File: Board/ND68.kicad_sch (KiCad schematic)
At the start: 4 parts

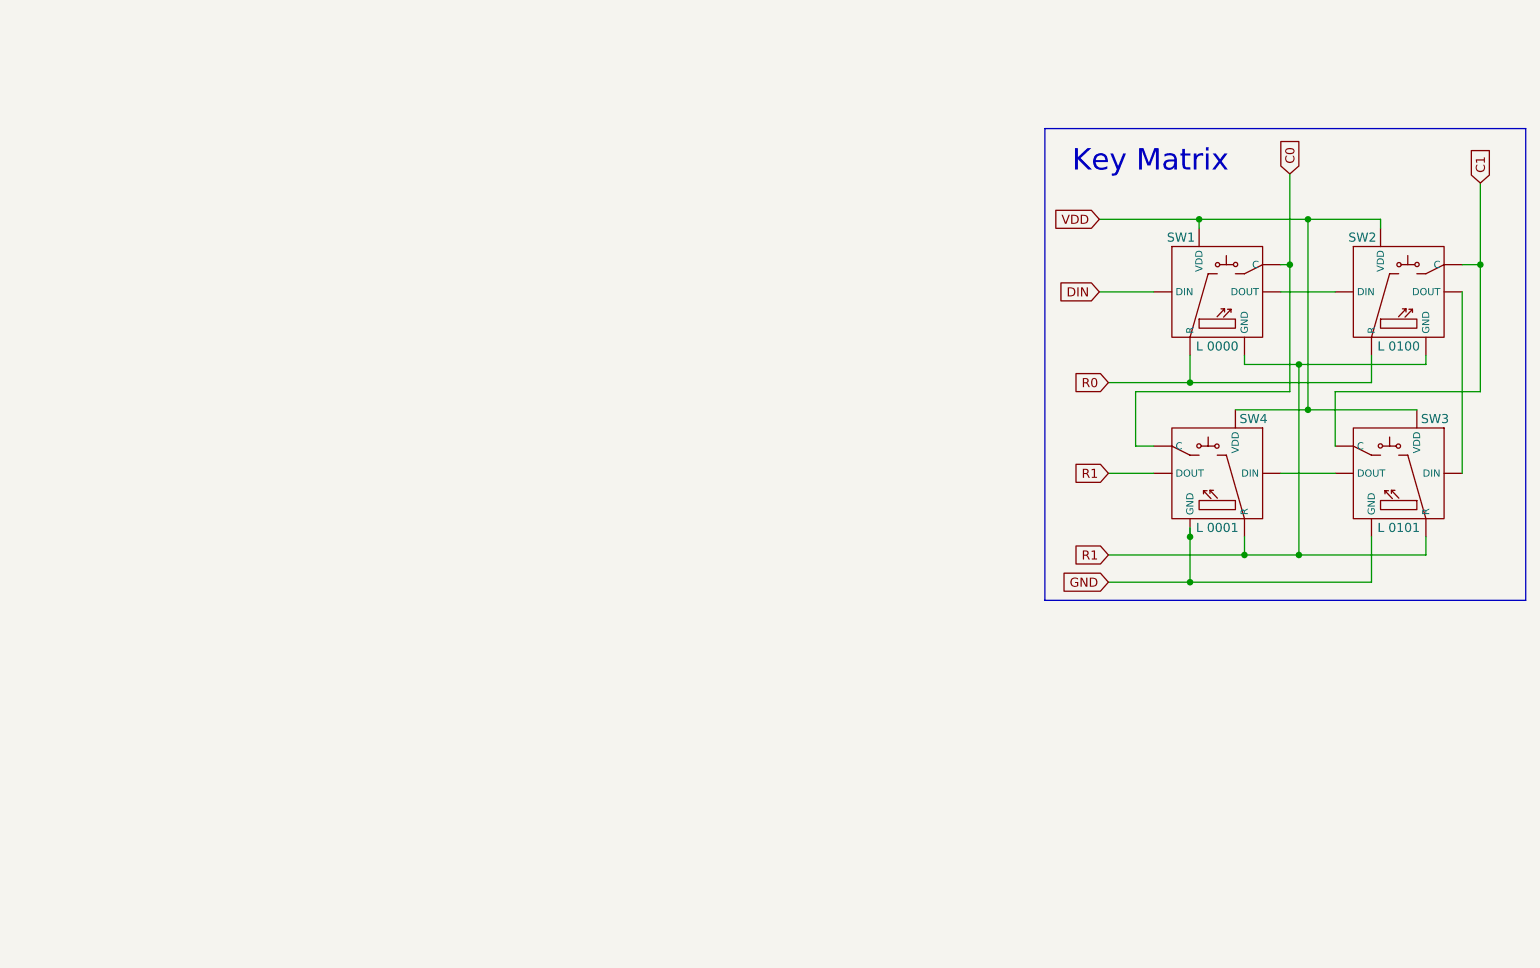
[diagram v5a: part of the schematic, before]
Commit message: Cleaned up key matrix and added diodes
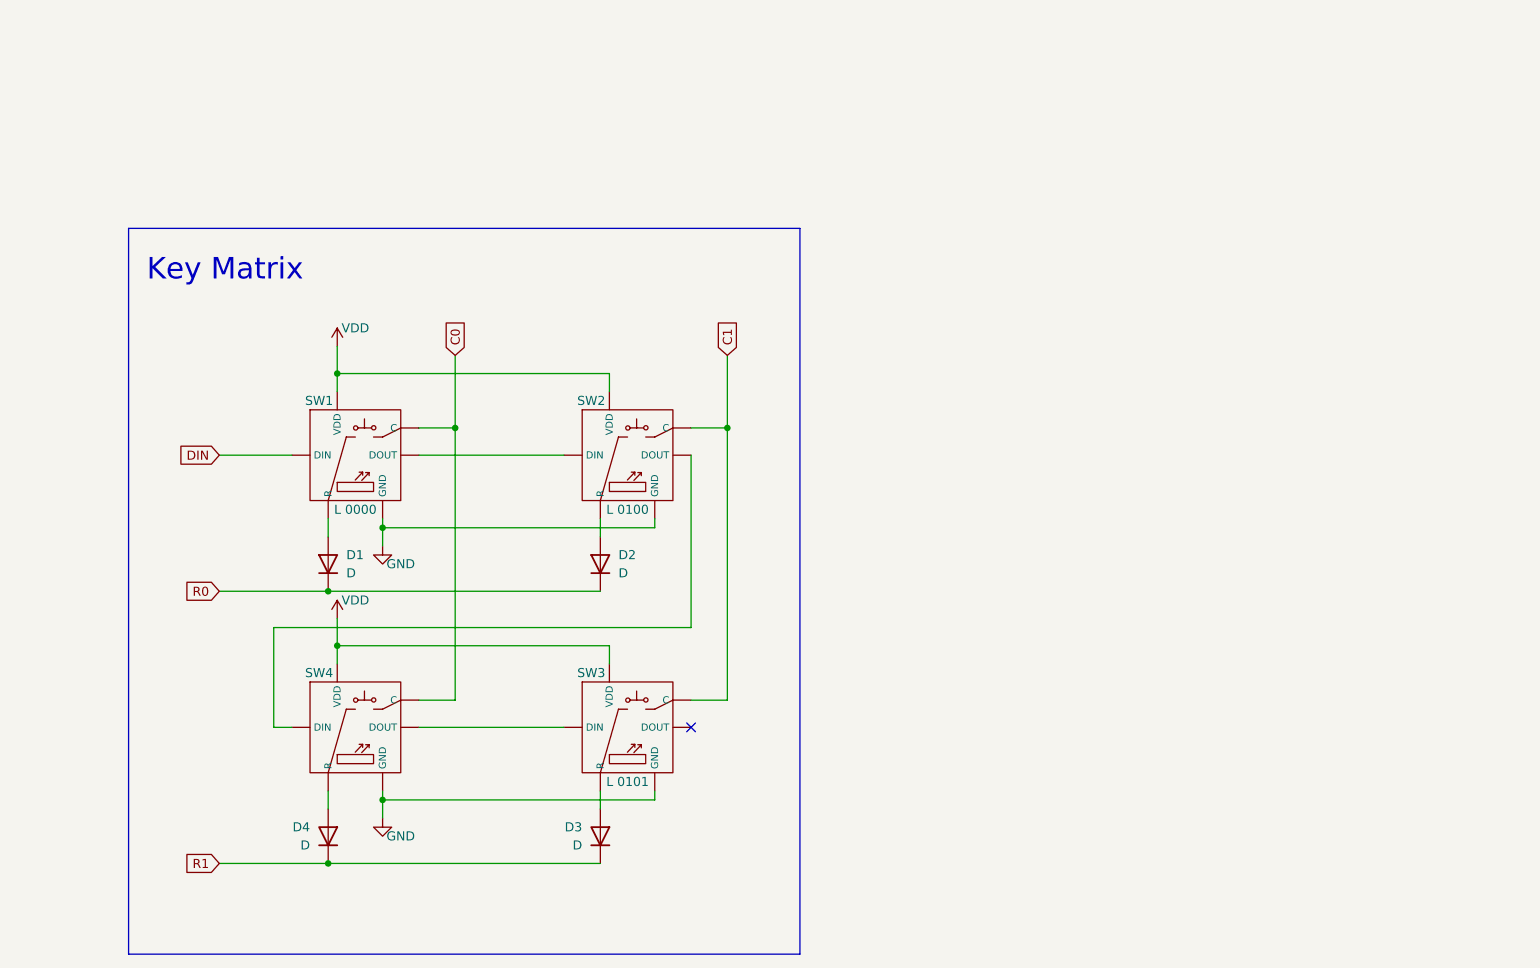
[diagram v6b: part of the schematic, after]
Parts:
- added D1, D2, D3, D4: D, Diode_SMD:D_SOD-123F, symbol Device:D
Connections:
- net GND: now also SW1. (VDD), SW2. (VDD)
- net R0: now also D1.1 (K), D2.1 (K); no longer SW1. (VDD), SW2. (VDD)
- net R1: now also D3.1 (K), D4.1 (K); no longer SW1. (VDD), SW2. (VDD), SW3. (VDD), SW4. (VDD)
- new net: SW3. (VDD), SW4. (VDD)
- new net: SW2. (VDD), SW4. (VDD)
- new net: D4.2 (A), SW4. (VDD)
- new net: D3.2 (A), SW3. (VDD)
- new net: D2.2 (A), SW2. (VDD)
- new net: D1.2 (A), SW1. (VDD)
- new net: SW1. (VDD), SW2. (VDD)
- no-connect marks 0 -> 1
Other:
- moved on the sheet: SW1, SW2, SW3, SW4

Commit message: Added 3d model to ND68-1u-HS-ARGB and linked all parts to footprints
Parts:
- SW1, SW2, SW3, SW4: footprint (none) -> ND68:ND68-1U-HS-ARGB
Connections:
- new net: SW3. (VDD), SW4. (VDD)
- new net: SW2. (VDD), SW4. (VDD)
- new net: SW1. (VDD), SW2. (VDD)
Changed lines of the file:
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@@
       (effects (font (size 1.27 1.27)))
     )
-    (property "Footprint" "" (at 120.65 115.57 0)
+    (property "Footprint" "ND68:ND68-1U-HS-ARGB" (at 120.65 115.57 0)
       (effects (font (size 1.27 1.27)) hide)
     )
@@
       (effects (font (size 1.27 1.27)))
     )
-    (property "Footprint" "" (at 158.75 115.57 0)
+    (property "Footprint" "ND68:ND68-1U-HS-ARGB" (at 158.75 115.57 0)
       (effects (font (size 1.27 1.27)) hide)
     )
@@
     )
     (property "Value" "D" (at 157.48 86.36 90)
-      (effects (font (size 1.27 1.27)) (justify right))
+      (effects (font (size 1.27 1.27)) (justify right) hide)
     )
     (property "Footprint" "Diode_SMD:D_SOD-123F" (at 154.94 85.09 0)
@@
     )
     (property "Value" "D" (at 152.4 124.46 90)
-      (effects (font (size 1.27 1.27)) (justify right))
+      (effects (font (size 1.27 1.27)) (justify right) hide)
     )
     (property "Footprint" "Diode_SMD:D_SOD-123F" (at 154.94 123.19 0)
@@
       (effects (font (size 1.27 1.27)))
     )
-    (property "Footprint" "" (at 120.65 77.47 0)
+    (property "Footprint" "ND68:ND68-1U-HS-ARGB" (at 120.65 77.47 0)
       (effects (font (size 1.27 1.27)) hide)
     )
@@
     )
     (property "Value" "D" (at 119.38 86.36 90)
-      (effects (font (size 1.27 1.27)) (justify right))
+      (effects (font (size 1.27 1.27)) (justify right) hide)
     )
     (property "Footprint" "Diode_SMD:D_SOD-123F" (at 116.84 85.09 0)
@@
       (effects (font (size 1.27 1.27)))
     )
-    (property "Footprint" "" (at 158.75 77.47 0)
+    (property "Footprint" "ND68:ND68-1U-HS-ARGB" (at 158.75 77.47 0)
       (effects (font (size 1.27 1.27)) hide)
     )
@@
     )
     (property "Value" "D" (at 114.3 124.46 90)
-      (effects (font (size 1.27 1.27)) (justify right))
+      (effects (font (size 1.27 1.27)) (justify right) hide)
     )
     (property "Footprint" "Diode_SMD:D_SOD-123F" (at 116.84 123.19 0)

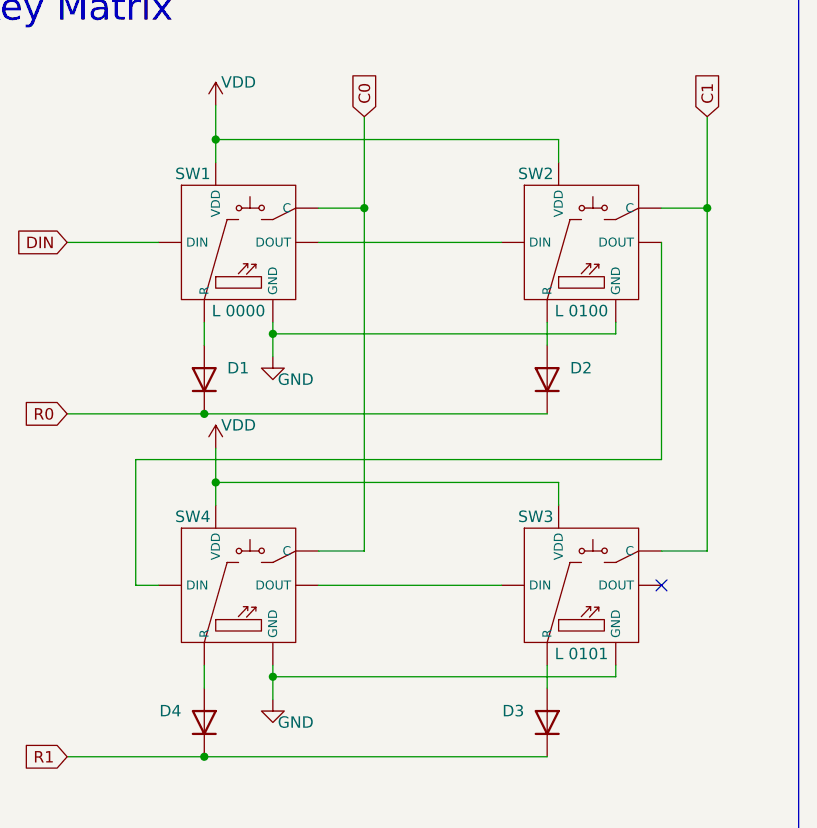
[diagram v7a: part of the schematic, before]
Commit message: Fixed pad numbers on 1u argb hotswap footprint and added a border to the pcb :)
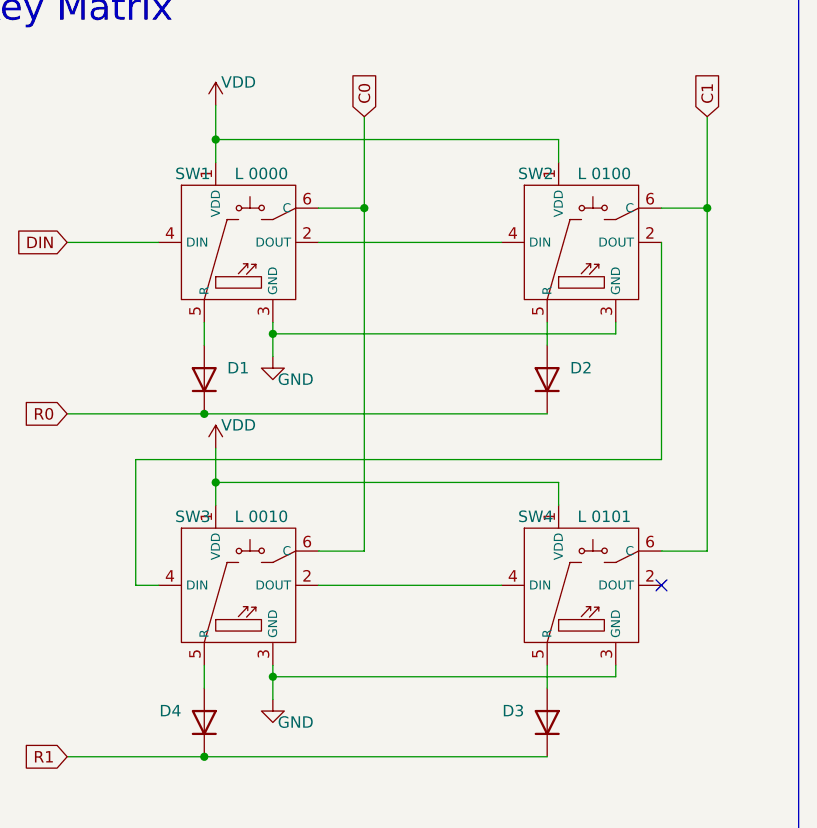
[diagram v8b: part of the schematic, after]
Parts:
- SW3: RC L 0101 -> L 0010
- SW4: RC L 0001 -> L 0101
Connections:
- net C0: now also SW1.6 (C), SW3.6 (C); no longer SW1. (VDD), SW4. (VDD)
- net C1: now also SW2.6 (C), SW4.6 (C); no longer SW2. (VDD), SW3. (VDD)
- net DIN: now also SW1.4 (DIN); no longer SW1. (VDD)
- net GND: now also SW1.3 (GND), SW2.3 (GND), SW3.3 (GND), SW4.3 (GND); no longer SW1. (VDD), SW2. (VDD), SW3. (VDD), SW4. (VDD)
- net VDD: now also SW1.1 (VDD), SW2.1 (VDD), SW3.1 (VDD), SW4.1 (VDD); no longer SW1. (VDD), SW2. (VDD), SW3. (VDD), SW4. (VDD)
- net at D4.2 (A): now also SW3.5 (R); no longer SW4. (VDD)
- net at D3.2 (A): now also SW4.5 (R); no longer SW3. (VDD)
- net at D2.2 (A): now also SW2.5 (R); no longer SW2. (VDD)
- net at D1.2 (A): now also SW1.5 (R); no longer SW1. (VDD)
- new net: SW3.2 (DOUT), SW4.4 (DIN)
- new net: SW2.2 (DOUT), SW3.4 (DIN)
- new net: SW1.2 (DOUT), SW2.4 (DIN)
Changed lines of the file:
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@@
+    )
+  )
+  (symbol (lib_id "ND68:nd68_hotswap_argb") (at 158.75 107.95 0) (unit 1)
+    (in_bom yes) (on_board yes) (dnp no) (fields_autoplaced)
+    (property "Reference" "SW4" (at 153.67 100.33 0) (do_not_autoplace)
+      (effects (font (size 1.27 1.27)))
+    )
+    (property "Value" "~" (at 158.75 115.57 0)
+      (effects (font (size 1.27 1.27)) hide)
+    )
+    (property "Footprint" "ND68:ND68-1U-HS-ARGB" (at 157.48 121.92 0)
+      (effects (font (size 1.27 1.27)) hide)
+    )
+    (property "Datasheet" "https://cdn-shop.adafruit.com/product-files/4960/4960_SK6812MINI-E_REV02_EN.pdf" (at 157.48 121.92 0)
+      (effects (font (size 1.27 1.27)) hide)
+    )
+    (property "RC" "L 0101" (at 161.29 100.33 0) (do_not_autoplace)
+      (effects (font (size 1.27 1.27)))
+    )
+    (pin "1")
+    (pin "2")
+    (pin "3")
+    (pin "4")
+    (pin "6")
+    (pin "5")
+    (instances
+      (project "ND68"
+        (path "/f6515d16-f8c0-46c5-adb6-b60d73ae282b"
+          (reference "SW4") (unit 1)
+        )
+      )
     )
   )
@@
     )
   )
-  (symbol (lib_id "ND68:nd68_hotswap_argb") (at 120.65 107.95 0) (unit 1)
-    (in_bom yes) (on_board yes) (dnp no) (fields_autoplaced)
-    (property "Reference" "SW4" (at 115.57 100.33 0) (do_not_autoplace)
-      (effects (font (size 1.27 1.27)))
-    )
-    (property "Value" "~" (at 120.65 115.57 0)
-      (effects (font (size 1.27 1.27)))
-    )
-    (property "Footprint" "ND68:ND68-1U-HS-ARGB" (at 120.65 115.57 0)
-      (effects (font (size 1.27 1.27)) hide)
-    )
-    (property "Datasheet" "" (at 120.65 115.57 0)
-      (effects (font (size 1.27 1.27)) hide)
-    )
-    (property "RC" "L 0001" (at 120.65 115.57 0) (do_not_autoplace)
-      (effects (font (size 1.27 1.27)) hide)
-    )
-    (pin "")
-    (pin "")
-    (pin "")
-    (pin "")
-    (pin "")
-    (pin "")
-    (instances
-      (project "ND68"
-        (path "/f6515d16-f8c0-46c5-adb6-b60d73ae282b"
-          (reference "SW4") (unit 1)
-        )
-      )
-    )
-  )
-  (symbol (lib_id "ND68:nd68_hotswap_argb") (at 158.75 107.95 0) (unit 1)
-    (in_bom yes) (on_board yes) (dnp no)
-    (property "Reference" "SW3" (at 153.67 100.33 0) (do_not_autoplace)
-      (effects (font (size 1.27 1.27)))
-    )
-    (property "Value" "~" (at 158.75 115.57 0)
-      (effects (font (size 1.27 1.27)))
-    )
-    (property "Footprint" "ND68:ND68-1U-HS-ARGB" (at 158.75 115.57 0)
-      (effects (font (size 1.27 1.27)) hide)
-    )
-    (property "Datasheet" "" (at 158.75 115.57 0)
-      (effects (font (size 1.27 1.27)) hide)
-    )
-    (property "RC" "L 0101" (at 158.75 115.57 0) (do_not_autoplace)
-      (effects (font (size 1.27 1.27)))
-    )
-    (pin "")
-    (pin "")
-    (pin "")
-    (pin "")
-    (pin "")
-    (pin "")
-    (instances
-      (project "ND68"
-        (path "/f6515d16-f8c0-46c5-adb6-b60d73ae282b"
-          (reference "SW3") (unit 1)
-        )
-      )
-    )
-  )
   (symbol (lib_id "Device:D") (at 154.94 85.09 90) (unit 1)
     (in_bom yes) (on_board yes) (dnp no) (fields_autoplaced)
@@
     )
   )
-  (symbol (lib_id "ND68:nd68_hotswap_argb") (at 120.65 69.85 0) (unit 1)
-    (in_bom yes) (on_board yes) (dnp no) (fields_autoplaced)
-    (property "Reference" "SW1" (at 115.57 62.23 0) (do_not_autoplace)
-      (effects (font (size 1.27 1.27)))
-    )
-    (property "Value" "~" (at 120.65 77.47 0)
-      (effects (font (size 1.27 1.27)))
-    )
-    (property "Footprint" "ND68:ND68-1U-HS-ARGB" (at 120.65 77.47 0)
-      (effects (font (size 1.27 1.27)) hide)
-    )
-    (property "Datasheet" "" (at 120.65 77.47 0)
-      (effects (font (size 1.27 1.27)) hide)
-    )
-    (property "RC" "L 0000" (at 120.65 77.47 0) (do_not_autoplace)
-      (effects (font (size 1.27 1.27)))
-    )
-    (pin "")
-    (pin "")
-    (pin "")
-    (pin "")
-    (pin "")
-    (pin "")
-    (instances
-      (project "ND68"
-        (path "/f6515d16-f8c0-46c5-adb6-b60d73ae282b"
-          (reference "SW1") (unit 1)
-        )
-      )
-    )
-  )
   (symbol (lib_id "Device:D") (at 116.84 85.09 90) (unit 1)
     (in_bom yes) (on_board yes) (dnp no) (fields_autoplaced)
@@
         (path "/f6515d16-f8c0-46c5-adb6-b60d73ae282b"
           (reference "D1") (unit 1)
+        )
+      )
+    )
+  )
+  (symbol (lib_id "ND68:nd68_hotswap_argb") (at 158.75 69.85 0) (unit 1)
+    (in_bom yes) (on_board yes) (dnp no) (fields_autoplaced)
+    (property "Reference" "SW2" (at 153.67 62.23 0) (do_not_autoplace)
+      (effects (font (size 1.27 1.27)))
+    )
+    (property "Value" "~" (at 158.75 77.47 0)
+      (effects (font (size 1.27 1.27)) hide)
+    )
+    (property "Footprint" "ND68:ND68-1U-HS-ARGB" (at 157.48 83.82 0)
+      (effects (font (size 1.27 1.27)) hide)
+    )
+    (property "Datasheet" "https://cdn-shop.adafruit.com/product-files/4960/4960_SK6812MINI-E_REV02_EN.pdf" (at 157.48 83.82 0)
+      (effects (font (size 1.27 1.27)) hide)
+    )
+    (property "RC" "L 0100" (at 161.29 62.23 0) (do_not_autoplace)
+      (effects (font (size 1.27 1.27)))
+    )
+    (pin "1")
+    (pin "2")
+    (pin "3")
+    (pin "4")
+    (pin "6")
+    (pin "5")
+    (instances
+      (project "ND68"
+        (path "/f6515d16-f8c0-46c5-adb6-b60d73ae282b"
+          (reference "SW2") (unit 1)
+        )
+      )
+    )
+  )
+  (symbol (lib_id "ND68:nd68_hotswap_argb") (at 120.65 107.95 0) (unit 1)
+    (in_bom yes) (on_board yes) (dnp no) (fields_autoplaced)
+    (property "Reference" "SW3" (at 115.57 100.33 0) (do_not_autoplace)
+      (effects (font (size 1.27 1.27)))
+    )
+    (property "Value" "~" (at 120.65 115.57 0)
+      (effects (font (size 1.27 1.27)) hide)
+    )
+    (property "Footprint" "ND68:ND68-1U-HS-ARGB" (at 119.38 121.92 0)
+      (effects (font (size 1.27 1.27)) hide)
+    )
+    (property "Datasheet" "https://cdn-shop.adafruit.com/product-files/4960/4960_SK6812MINI-E_REV02_EN.pdf" (at 119.38 121.92 0)
+      (effects (font (size 1.27 1.27)) hide)
+    )
+    (property "RC" "L 0010" (at 123.19 100.33 0) (do_not_autoplace)
+      (effects (font (size 1.27 1.27)))
+    )
+    (pin "1")
+    (pin "2")
+    (pin "3")
+    (pin "4")
+    (pin "6")
+    (pin "5")
+    (instances
+      (project "ND68"
+        (path "/f6515d16-f8c0-46c5-adb6-b60d73ae282b"
+          (reference "SW3") (unit 1)
+        )
+      )
+    )
+  )
+  (symbol (lib_id "ND68:nd68_hotswap_argb") (at 120.65 69.85 0) (unit 1)
+    (in_bom yes) (on_board yes) (dnp no) (fields_autoplaced)
+    (property "Reference" "SW1" (at 115.57 62.23 0) (do_not_autoplace)
+      (effects (font (size 1.27 1.27)))
+    )
+    (property "Value" "~" (at 120.65 77.47 0)
+      (effects (font (size 1.27 1.27)) hide)
+    )
+    (property "Footprint" "ND68:ND68-1U-HS-ARGB" (at 119.38 83.82 0)
+      (effects (font (size 1.27 1.27)) hide)
+    )
+    (property "Datasheet" "https://cdn-shop.adafruit.com/product-files/4960/4960_SK6812MINI-E_REV02_EN.pdf" (at 119.38 83.82 0)
+      (effects (font (size 1.27 1.27)) hide)
+    )
+    (property "RC" "L 0000" (at 123.19 62.23 0) (do_not_autoplace)
+      (effects (font (size 1.27 1.27)))
+    )
+    (pin "1")
+    (pin "2")
+    (pin "3")
+    (pin "4")
+    (pin "6")
+    (pin "5")
+    (instances
+      (project "ND68"
+        (path "/f6515d16-f8c0-46c5-adb6-b60d73ae282b"
+          (reference "SW1") (unit 1)
         )
       )
@@
         )
       )
-    )
-  )
-  (symbol (lib_id "ND68:nd68_hotswap_argb") (at 158.75 69.85 0) (unit 1)
-    (in_bom yes) (on_board yes) (dnp no) (fields_autoplaced)
-    (property "Reference" "SW2" (at 153.67 62.23 0) (do_not_autoplace)
-      (effects (font (size 1.27 1.27)))
-    )
-    (property "Value" "~" (at 158.75 77.47 0)
-      (effects (font (size 1.27 1.27)))
-    )
-    (property "Footprint" "ND68:ND68-1U-HS-ARGB" (at 158.75 77.47 0)
-      (effects (font (size 1.27 1.27)) hide)
-    )
-    (property "Datasheet" "" (at 158.75 77.47 0)
-      (effects (font (size 1.27 1.27)) hide)
-    )
-    (property "RC" "L 0100" (at 158.75 77.47 0) (do_not_autoplace)
-      (effects (font (size 1.27 1.27)))
-    )
-    (pin "")
-    (pin "")
-    (pin "")
-    (pin "")
-    (pin "")
-    (pin "")
-    (instances
-      (project "ND68"
-        (path "/f6515d16-f8c0-46c5-adb6-b60d73ae282b"
-          (reference "SW2") (unit 1)
-        )
-      )
